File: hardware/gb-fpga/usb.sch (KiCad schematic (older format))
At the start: 14 parts, among them J1 USB_C_Receptacle_USB2.0, U3 FT2232HQ, X1 SG-8002JA

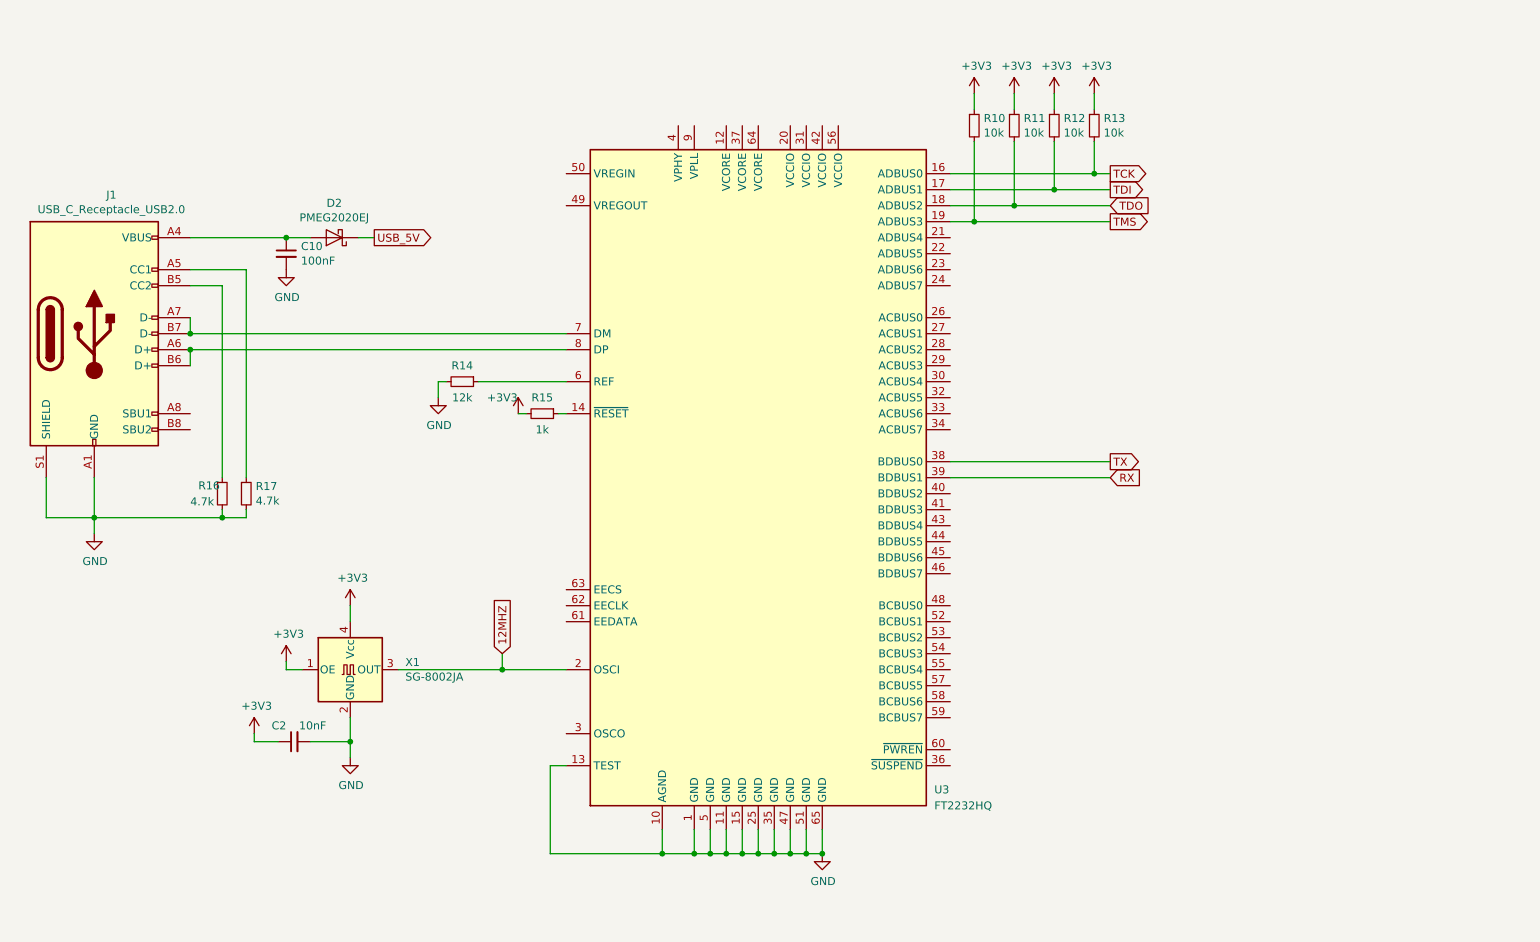
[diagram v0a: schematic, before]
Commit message: Add missing power supplies
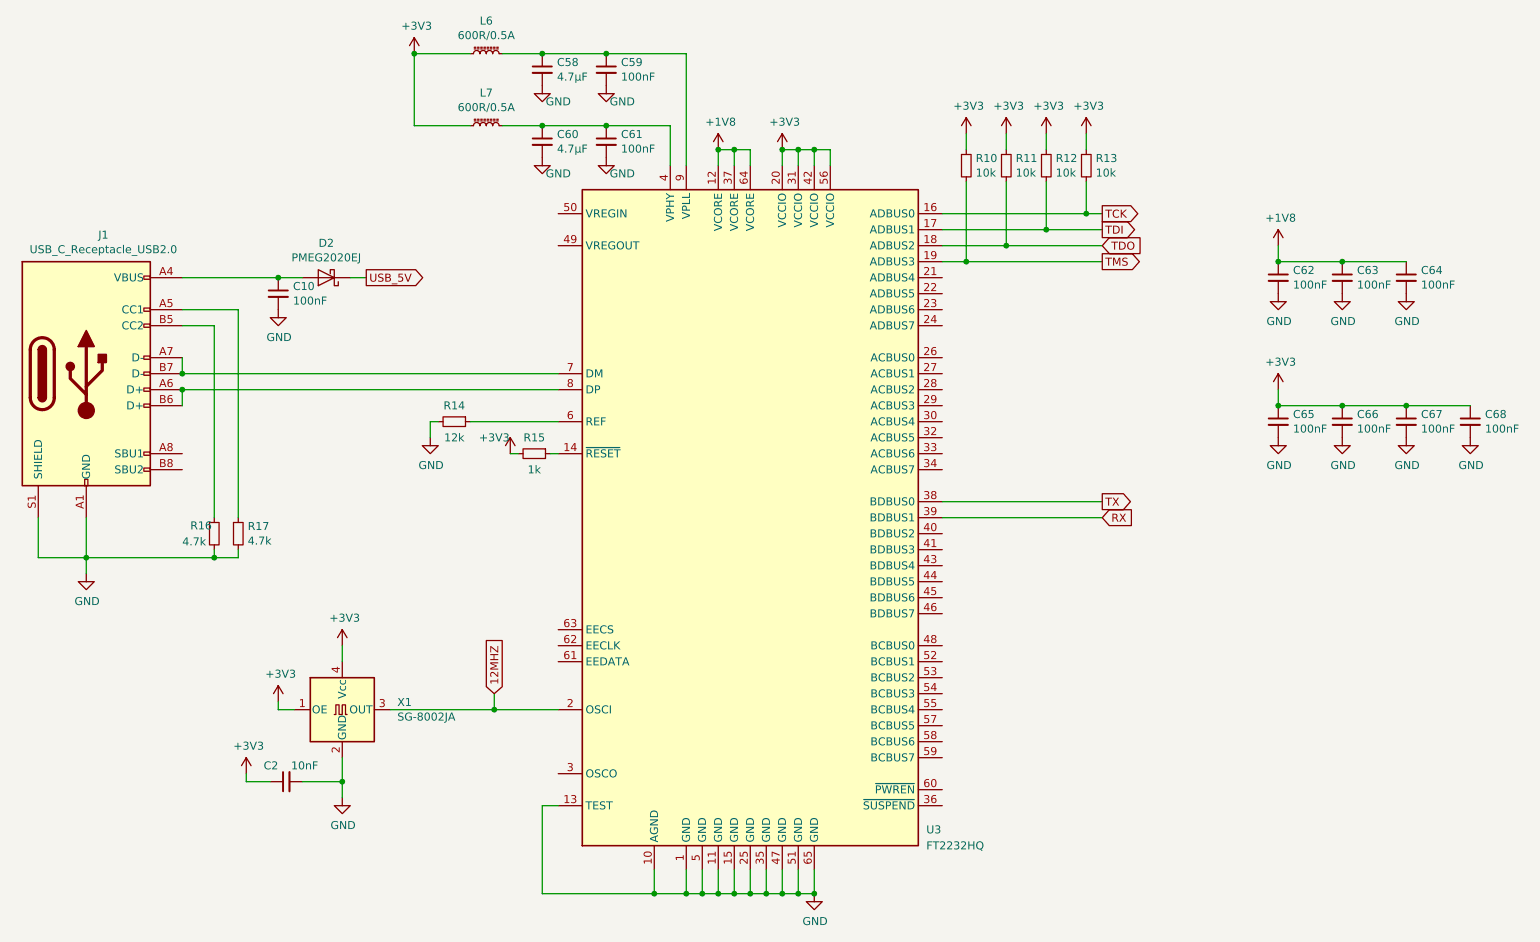
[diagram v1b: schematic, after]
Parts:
- added C58, C60: 4.7µF, Capacitor_SMD:C_0402_1005Metric, symbol Device:C_Small
- added C59, C61, C62, C63, C64, C65, C66, C67, C68: 100nF, Capacitor_SMD:C_0402_1005Metric, symbol Device:C_Small
- added L6, L7: 600R/0.5A, Inductor_SMD:L_0402_1005Metric, symbol Device:L_Core_Ferrite_Small
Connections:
- net +3V3: now also U3.20 (VCCIO), U3.31 (VCCIO), U3.42 (VCCIO), U3.56 (VCCIO), C65.1, C66.1, C67.1, C68.1, L6.1, L7.1
- net GND: now also C58.2, C59.2, C60.2, C61.2, C62.2, C63.2, C64.2, C65.2, C66.2, C67.2, C68.2
- net +1V8: now reaches U3.12 (VCORE)
- net +1V8: now also U3.37 (VCORE), U3.64 (VCORE), C62.1, C63.1, C64.1
- net at U3.4 (VPHY): now also C60.1, C61.1, L7.2
- net at U3.9 (VPLL): now also C58.1, C59.1, L6.2
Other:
- moved on the sheet: C10, C2, D2, J1, R10, R11, R12, R13, R14, R15, R16, R17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

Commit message: Update bom
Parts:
- C10, C59, C61, C62, C63, C64, C65, C66, C67, C68: Manufacturer Part Number (none) -> CL05B104KO5NNNC
- C2: Manufacturer Part Number (none) -> CL05B103KB5NNNC
- C58, C60: Manufacturer Part Number (none) -> CL05A475KP5NRNC
- D2: Manufacturer Part Number (none) -> PMEG2020EJF
- J1: Manufacturer Part Number (none) -> U262-161N-4BVC11
- L6, L7: Manufacturer Part Number (none) -> BLM15AX601SN1D
- R10, R11, R12, R13: Manufacturer Part Number (none) -> RC0402JR-0710KL
- R14: Manufacturer Part Number (none) -> RC0402FR-0712KL
- R15: Manufacturer Part Number (none) -> RC0402JR-071KL
- R16, R17: Manufacturer Part Number (none) -> RC0402JR-074K7L
- U3: Manufacturer Part Number (none) -> FT2232HQ-REEL
- X1: Manufacturer Part Number (none) -> CB3LV-3C-12M000000
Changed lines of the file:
@@
 F 2 "Package_DFN_QFN:QFN-64-1EP_9x9mm_P0.5mm_EP4.35x4.35mm" H 5800 4050 50  0001 C CNN
 F 3 "https://www.ftdichip.com/Support/Documents/DataSheets/ICs/DS_FT2232H.pdf" H 5800 4050 50  0001 C CNN
+F 4 "FT2232HQ-REEL" H 5800 4050 50  0001 C CNN "Manufacturer Part Number"
 	1    5800 4050
 	1    0    0    -1
@@
 F 2 "Connector_USB:USB_C_Receptacle_XKB_U262-16XN-4BVC11" H 1800 3150 50  0001 C CNN
 F 3 "https://www.usb.org/sites/default/files/documents/usb_type-c.zip" H 1800 3150 50  0001 C CNN
+F 4 "U262-161N-4BVC11" H 1650 3150 50  0001 C CNN "Manufacturer Part Number"
 	1    1650 3150
 	1    0    0    -1
@@
 F 2 "Resistor_SMD:R_0402_1005Metric" H 2600 4150 50  0001 C CNN
 F 3 "~" H 2600 4150 50  0001 C CNN
+F 4 "RC0402JR-074K7L" H 2600 4150 50  0001 C CNN "Manufacturer Part Number"
 	1    2600 4150
 	1    0    0    -1
@@
 F 2 "Resistor_SMD:R_0402_1005Metric" H 2450 4150 50  0001 C CNN
 F 3 "~" H 2450 4150 50  0001 C CNN
+F 4 "RC0402JR-074K7L" H 2450 4150 50  0001 C CNN "Manufacturer Part Number"
 	1    2450 4150
 	1    0    0    -1
@@
 F 2 "Resistor_SMD:R_0402_1005Metric" H 3950 3450 50  0001 C CNN
 F 3 "~" H 3950 3450 50  0001 C CNN
+F 4 "RC0402FR-0712KL" H 3950 3450 50  0001 C CNN "Manufacturer Part Number"
 	1    3950 3450
 	0    1    1    0
@@
 F 2 "Resistor_SMD:R_0402_1005Metric" H 4450 3650 50  0001 C CNN
 F 3 "~" H 4450 3650 50  0001 C CNN
+F 4 "RC0402JR-071KL" H 4450 3650 50  0001 C CNN "Manufacturer Part Number"
 	1    4450 3650
 	0    1    1    0
@@
 F 2 "Resistor_SMD:R_0402_1005Metric" H 7150 1850 50  0001 C CNN
 F 3 "~" H 7150 1850 50  0001 C CNN
+F 4 "RC0402JR-0710KL" H 7150 1850 50  0001 C CNN "Manufacturer Part Number"
 	1    7150 1850
 	1    0    0    -1
@@
 F 2 "Resistor_SMD:R_0402_1005Metric" H 7400 1850 50  0001 C CNN
 F 3 "~" H 7400 1850 50  0001 C CNN
+F 4 "RC0402JR-0710KL" H 7400 1850 50  0001 C CNN "Manufacturer Part Number"
 	1    7400 1850
 	1    0    0    -1
@@
 F 2 "Resistor_SMD:R_0402_1005Metric" H 7650 1850 50  0001 C CNN
 F 3 "~" H 7650 1850 50  0001 C CNN
+F 4 "RC0402JR-0710KL" H 7650 1850 50  0001 C CNN "Manufacturer Part Number"
 	1    7650 1850
 	1    0    0    -1
@@
 F 2 "Resistor_SMD:R_0402_1005Metric" H 7900 1850 50  0001 C CNN
 F 3 "~" H 7900 1850 50  0001 C CNN
+F 4 "RC0402JR-0710KL" H 7900 1850 50  0001 C CNN "Manufacturer Part Number"
 	1    7900 1850
 	1    0    0    -1
@@
 F 2 "Oscillator:Oscillator_SMD_Abracon_ASE-4Pin_3.2x2.5mm" H 3950 4900 50  0001 C CNN
 F 3 "https://support.epson.biz/td/api/doc_check.php?mode=dl&lang=en&Parts=SG-8002DC" H 3150 5250 50  0001 C CNN
+F 4 "CB3LV-3C-12M000000" H 3250 5250 50  0001 C CNN "Manufacturer Part Number"
 	1    3250 5250
 	1    0    0    -1
@@
 F 2 "Capacitor_SMD:C_0402_1005Metric" H 2900 5700 50  0001 C CNN
 F 3 "~" H 2900 5700 50  0001 C CNN
+F 4 "CL05B103KB5NNNC" H 2900 5700 50  0001 C CNN "Manufacturer Part Number"
 	1    2900 5700
 	0    -1   -1   0
@@
 F 2 "Diode_SMD:D_SOD-323F" H 3150 2375 50  0001 C CNN
 F 3 "https://assets.nexperia.com/documents/data-sheet/PMEG2020EH_EJ.pdf" H 3150 2550 50  0001 C CNN
+F 4 "PMEG2020EJF" H 3150 2550 50  0001 C CNN "Manufacturer Part Number"
 	1    3150 2550
 	-1   0    0    1
@@
 F 2 "Capacitor_SMD:C_0402_1005Metric" H 2850 2650 50  0001 C CNN
 F 3 "~" H 2850 2650 50  0001 C CNN
+F 4 "CL05B104KO5NNNC" H 2850 2650 50  0001 C CNN "Manufacturer Part Number"
 	1    2850 2650
 	1    0    0    -1
@@
 F 2 "Inductor_SMD:L_0402_1005Metric" H 4150 1600 50  0001 C CNN
 F 3 "~" H 4150 1600 50  0001 C CNN
+F 4 "BLM15AX601SN1D" H 4150 1600 50  0001 C CNN "Manufacturer Part Number"
 	1    4150 1600
 	0    -1   -1   0
@@
 F 2 "Inductor_SMD:L_0402_1005Metric" H 4150 1150 50  0001 C CNN
 F 3 "~" H 4150 1150 50  0001 C CNN
+F 4 "BLM15AX601SN1D" H 4150 1150 50  0001 C CNN "Manufacturer Part Number"
 	1    4150 1150
 	0    -1   -1   0
@@
 F 2 "Capacitor_SMD:C_0402_1005Metric" H 4500 1700 50  0001 C CNN
 F 3 "~" H 4500 1700 50  0001 C CNN
+F 4 "CL05A475KP5NRNC" H 4500 1700 50  0001 C CNN "Manufacturer Part Number"
 	1    4500 1700
 	1    0    0    -1
@@
 F 2 "Capacitor_SMD:C_0402_1005Metric" H 4900 1700 50  0001 C CNN
 F 3 "~" H 4900 1700 50  0001 C CNN
+F 4 "CL05B104KO5NNNC" H 4900 1700 50  0001 C CNN "Manufacturer Part Number"
 	1    4900 1700
 	1    0    0    -1
@@
 F 2 "Capacitor_SMD:C_0402_1005Metric" H 4500 1250 50  0001 C CNN
 F 3 "~" H 4500 1250 50  0001 C CNN
+F 4 "CL05A475KP5NRNC" H 4500 1250 50  0001 C CNN "Manufacturer Part Number"
 	1    4500 1250
 	1    0    0    -1
@@
 F 2 "Capacitor_SMD:C_0402_1005Metric" H 4900 1250 50  0001 C CNN
 F 3 "~" H 4900 1250 50  0001 C CNN
+F 4 "CL05B104KO5NNNC" H 4900 1250 50  0001 C CNN "Manufacturer Part Number"
 	1    4900 1250
 	1    0    0    -1
@@
 F 2 "Capacitor_SMD:C_0402_1005Metric" H 9100 2550 50  0001 C CNN
 F 3 "~" H 9100 2550 50  0001 C CNN
+F 4 "CL05B104KO5NNNC" H 9100 2550 50  0001 C CNN "Manufacturer Part Number"
 	1    9100 2550
 	1    0    0    -1
@@
 F 2 "Capacitor_SMD:C_0402_1005Metric" H 9500 2550 50  0001 C CNN
 F 3 "~" H 9500 2550 50  0001 C CNN
+F 4 "CL05B104KO5NNNC" H 9500 2550 50  0001 C CNN "Manufacturer Part Number"
 	1    9500 2550
 	1    0    0    -1
@@
 F 2 "Capacitor_SMD:C_0402_1005Metric" H 9900 2550 50  0001 C CNN
 F 3 "~" H 9900 2550 50  0001 C CNN
+F 4 "CL05B104KO5NNNC" H 9900 2550 50  0001 C CNN "Manufacturer Part Number"
 	1    9900 2550
 	1    0    0    -1
@@
 F 2 "Capacitor_SMD:C_0402_1005Metric" H 9100 3450 50  0001 C CNN
 F 3 "~" H 9100 3450 50  0001 C CNN
+F 4 "CL05B104KO5NNNC" H 9100 3450 50  0001 C CNN "Manufacturer Part Number"
 	1    9100 3450
 	1    0    0    -1
@@
 F 2 "Capacitor_SMD:C_0402_1005Metric" H 9500 3450 50  0001 C CNN
 F 3 "~" H 9500 3450 50  0001 C CNN
+F 4 "CL05B104KO5NNNC" H 9500 3450 50  0001 C CNN "Manufacturer Part Number"
 	1    9500 3450
 	1    0    0    -1
@@
 F 2 "Capacitor_SMD:C_0402_1005Metric" H 9900 3450 50  0001 C CNN
 F 3 "~" H 9900 3450 50  0001 C CNN
+F 4 "CL05B104KO5NNNC" H 9900 3450 50  0001 C CNN "Manufacturer Part Number"
 	1    9900 3450
 	1    0    0    -1
@@
 F 2 "Capacitor_SMD:C_0402_1005Metric" H 10300 3450 50  0001 C CNN
 F 3 "~" H 10300 3450 50  0001 C CNN
+F 4 "CL05B104KO5NNNC" H 10300 3450 50  0001 C CNN "Manufacturer Part Number"
 	1    10300 3450
 	1    0    0    -1

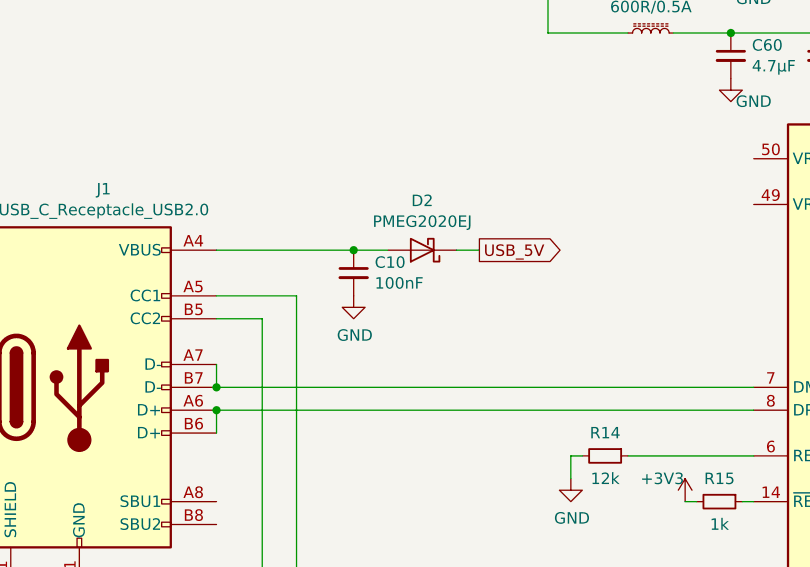
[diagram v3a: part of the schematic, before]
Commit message: Update footprints and BOM
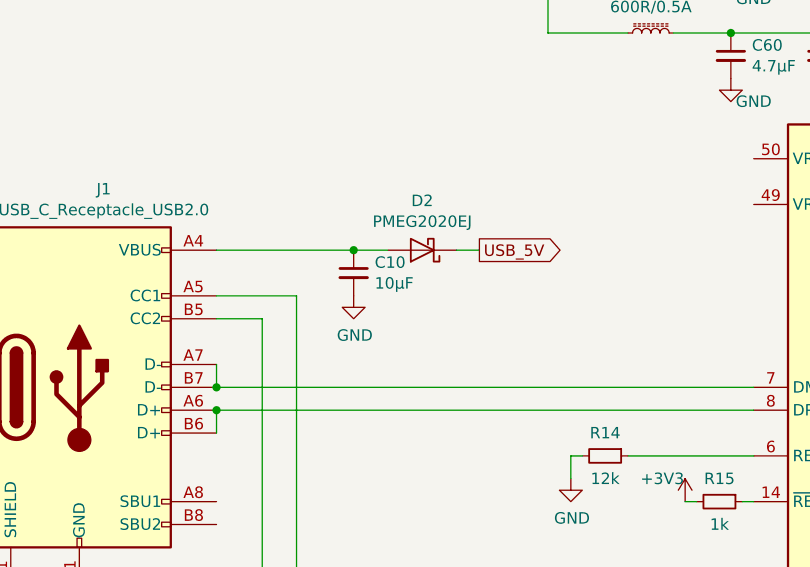
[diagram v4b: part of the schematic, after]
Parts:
- C10: value 100nF -> 10µF; Manufacturer Part Number CL05B104KO5NNNC -> CL05A106MP5NUNC
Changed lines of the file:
@@
 P 2850 2650
 F 0 "C10" H 2942 2696 50  0000 L CNN
-F 1 "100nF" H 2942 2605 50  0000 L CNN
+F 1 "10µF" H 2942 2605 50  0000 L CNN
 F 2 "Capacitor_SMD:C_0402_1005Metric" H 2850 2650 50  0001 C CNN
 F 3 "~" H 2850 2650 50  0001 C CNN
-F 4 "CL05B104KO5NNNC" H 2850 2650 50  0001 C CNN "Manufacturer Part Number"
+F 4 "CL05A106MP5NUNC" H 2850 2650 50  0001 C CNN "Manufacturer Part Number"
 	1    2850 2650
 	1    0    0    -1
